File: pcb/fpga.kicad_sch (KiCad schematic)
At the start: 45 parts, among them U1 XC7A50T-FTG256, U2 410-251-B, U3 S70KL1283GABHI020, U4 W25Q128JVS, Y1 ASE-20MHz

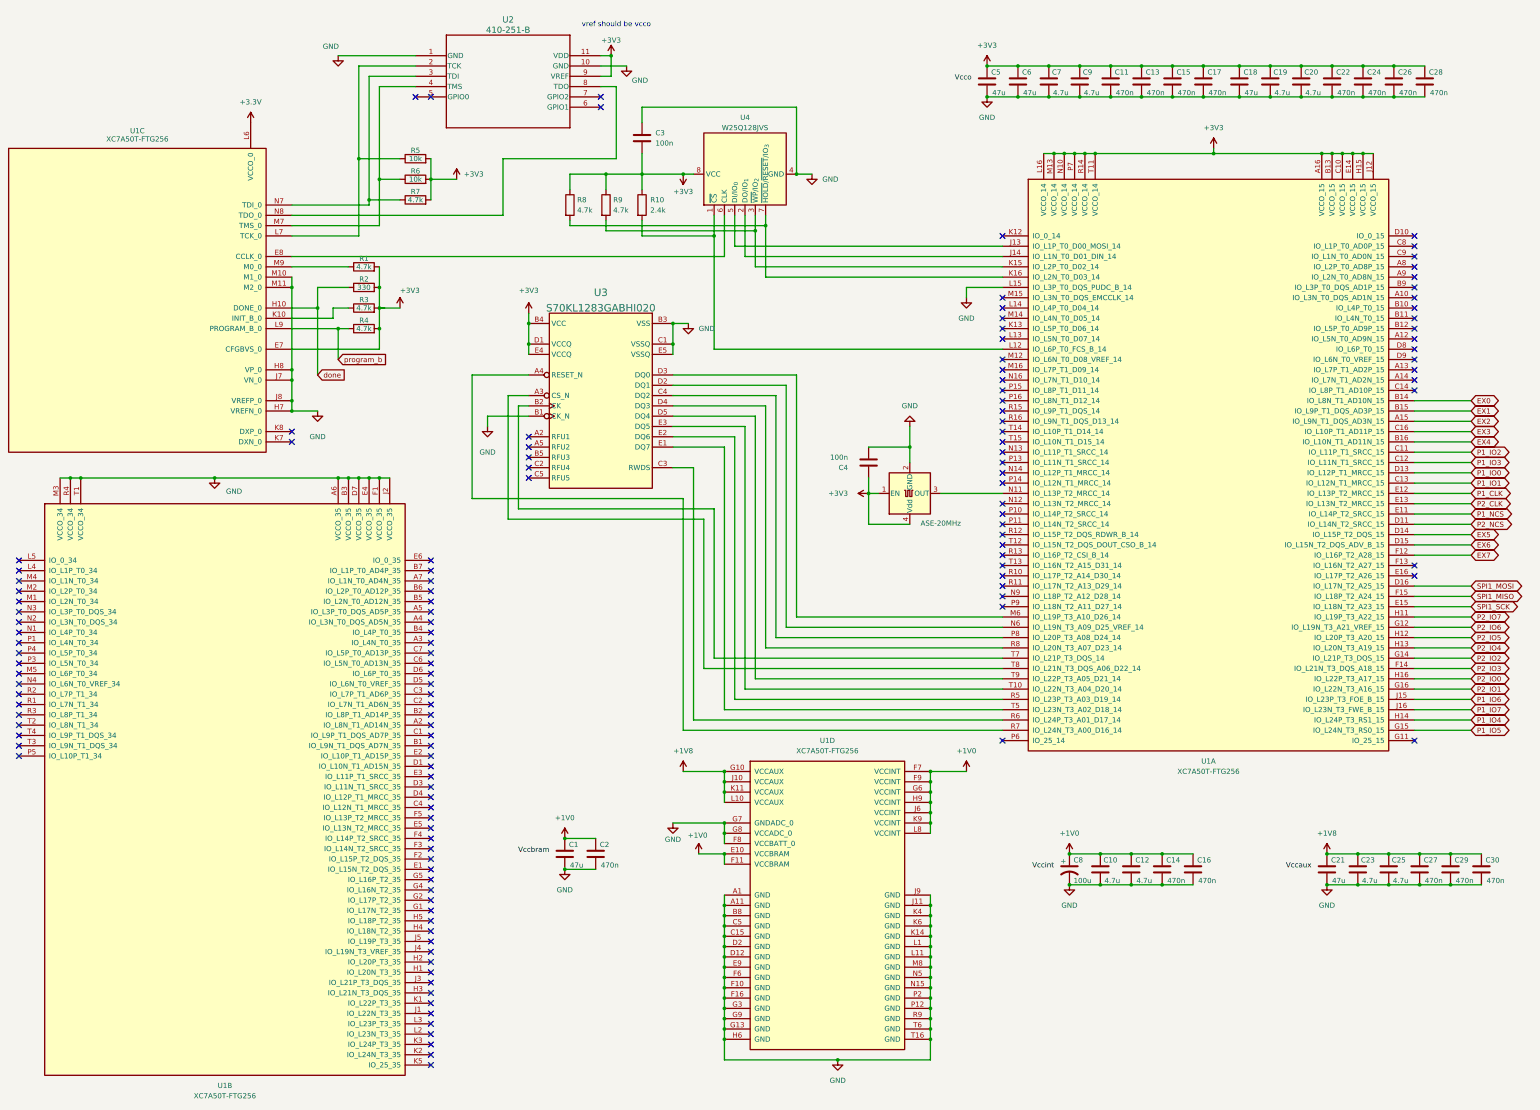
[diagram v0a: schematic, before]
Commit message: fixed erc errors
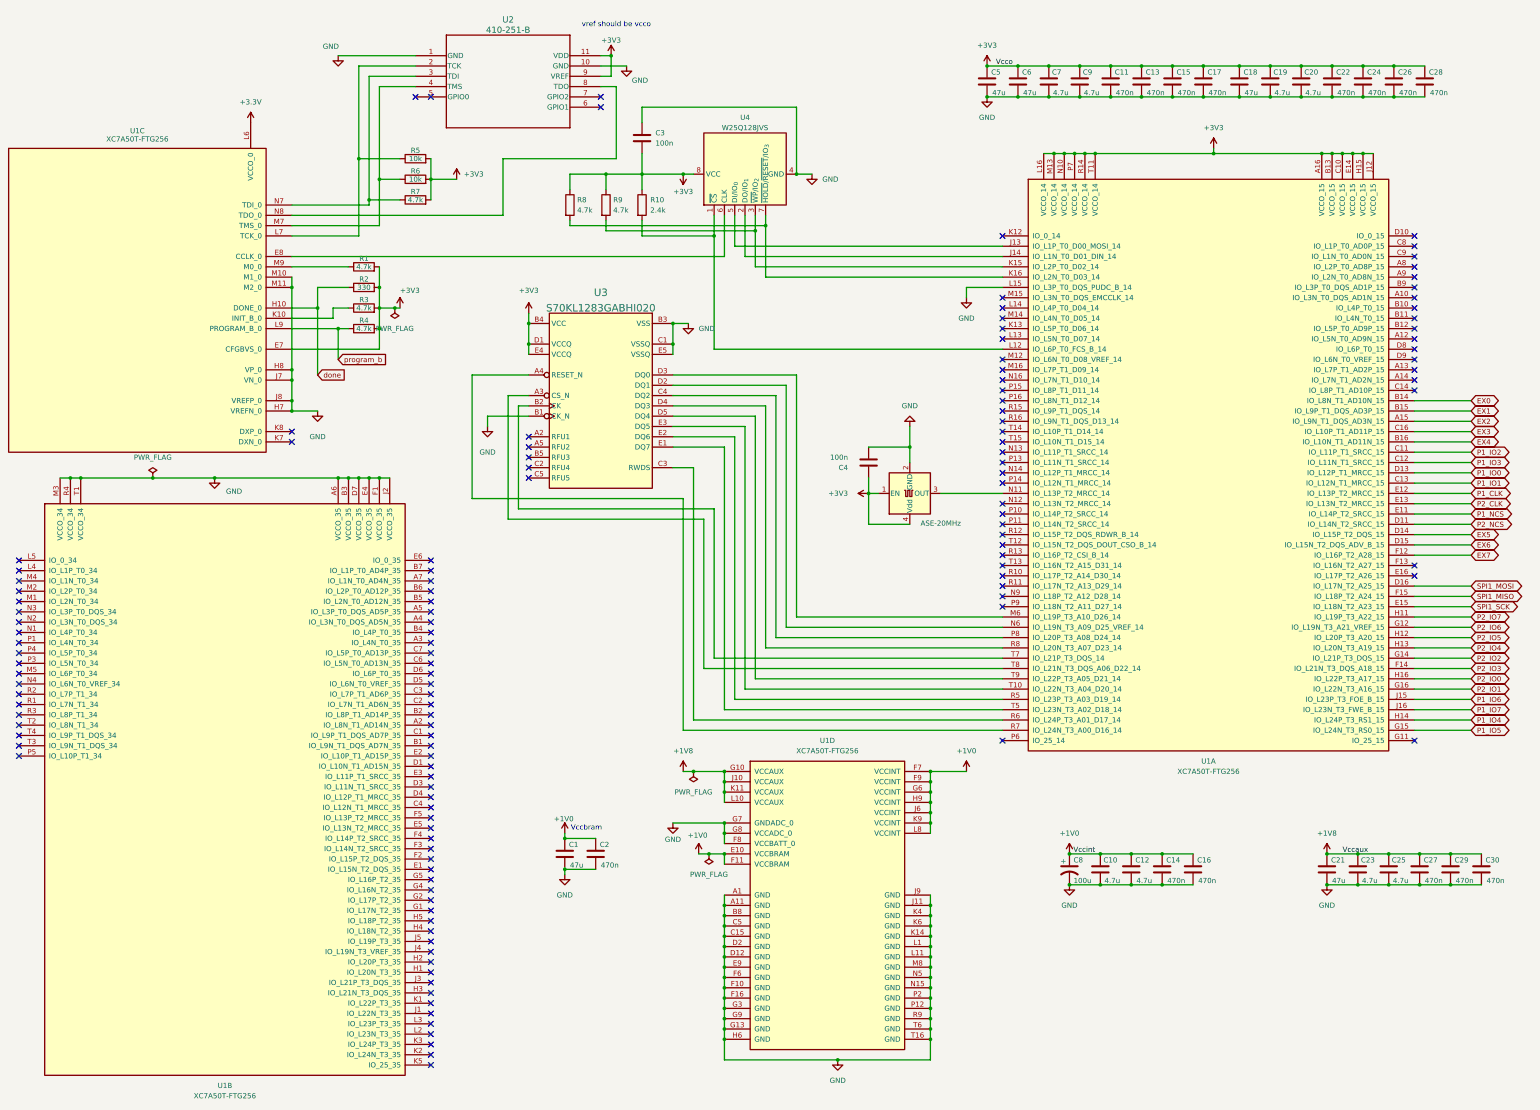
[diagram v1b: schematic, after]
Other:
- note added: "Vccbram"

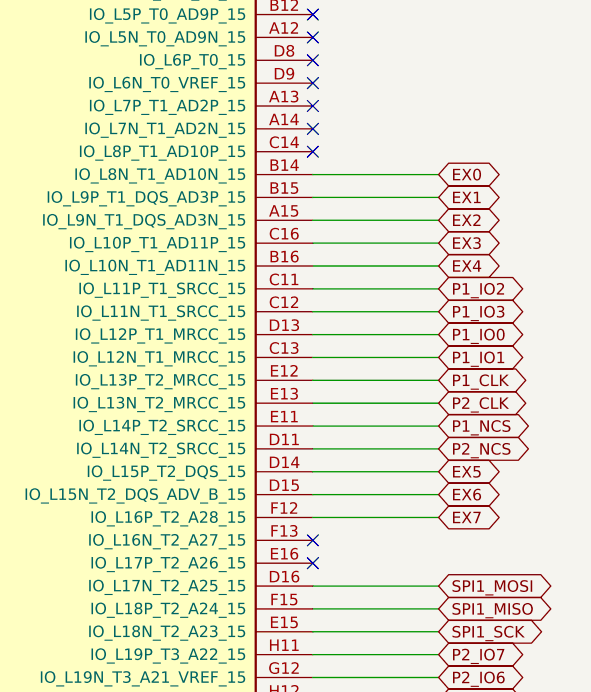
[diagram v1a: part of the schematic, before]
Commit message: pcb: fix erc
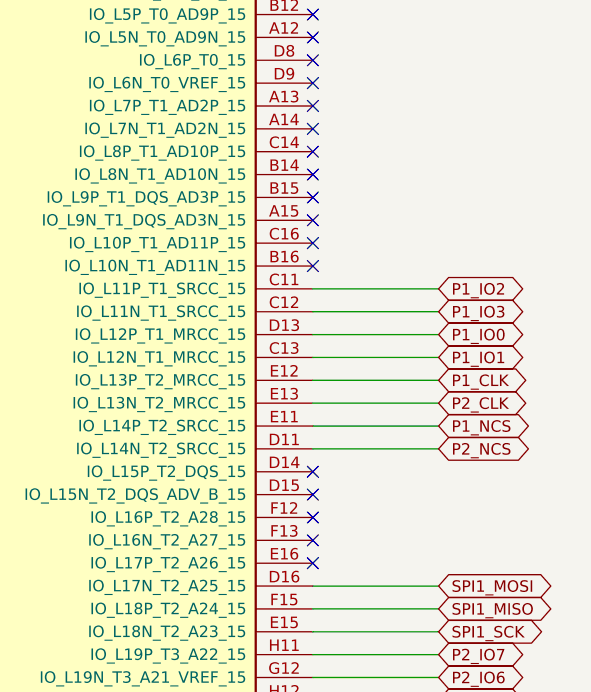
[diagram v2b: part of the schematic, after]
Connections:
- net EX0: no longer names the net of U1.B14 (IO_L8N_T1_AD10N_15)
- net EX1: no longer names the net of U1.B15 (IO_L9P_T1_DQS_AD3P_15)
- net EX2: no longer names the net of U1.A15 (IO_L9N_T1_DQS_AD3N_15)
- net EX3: no longer names the net of U1.C16 (IO_L10P_T1_AD11P_15)
- net EX4: no longer names the net of U1.B16 (IO_L10N_T1_AD11N_15)
- net EX5: no longer names the net of U1.D14 (IO_L15P_T2_DQS_15)
- net EX6: no longer names the net of U1.D15 (IO_L15N_T2_DQS_ADV_B_15)
- net EX7: no longer names the net of U1.F12 (IO_L16P_T2_A28_15)
- no-connect marks 131 -> 139

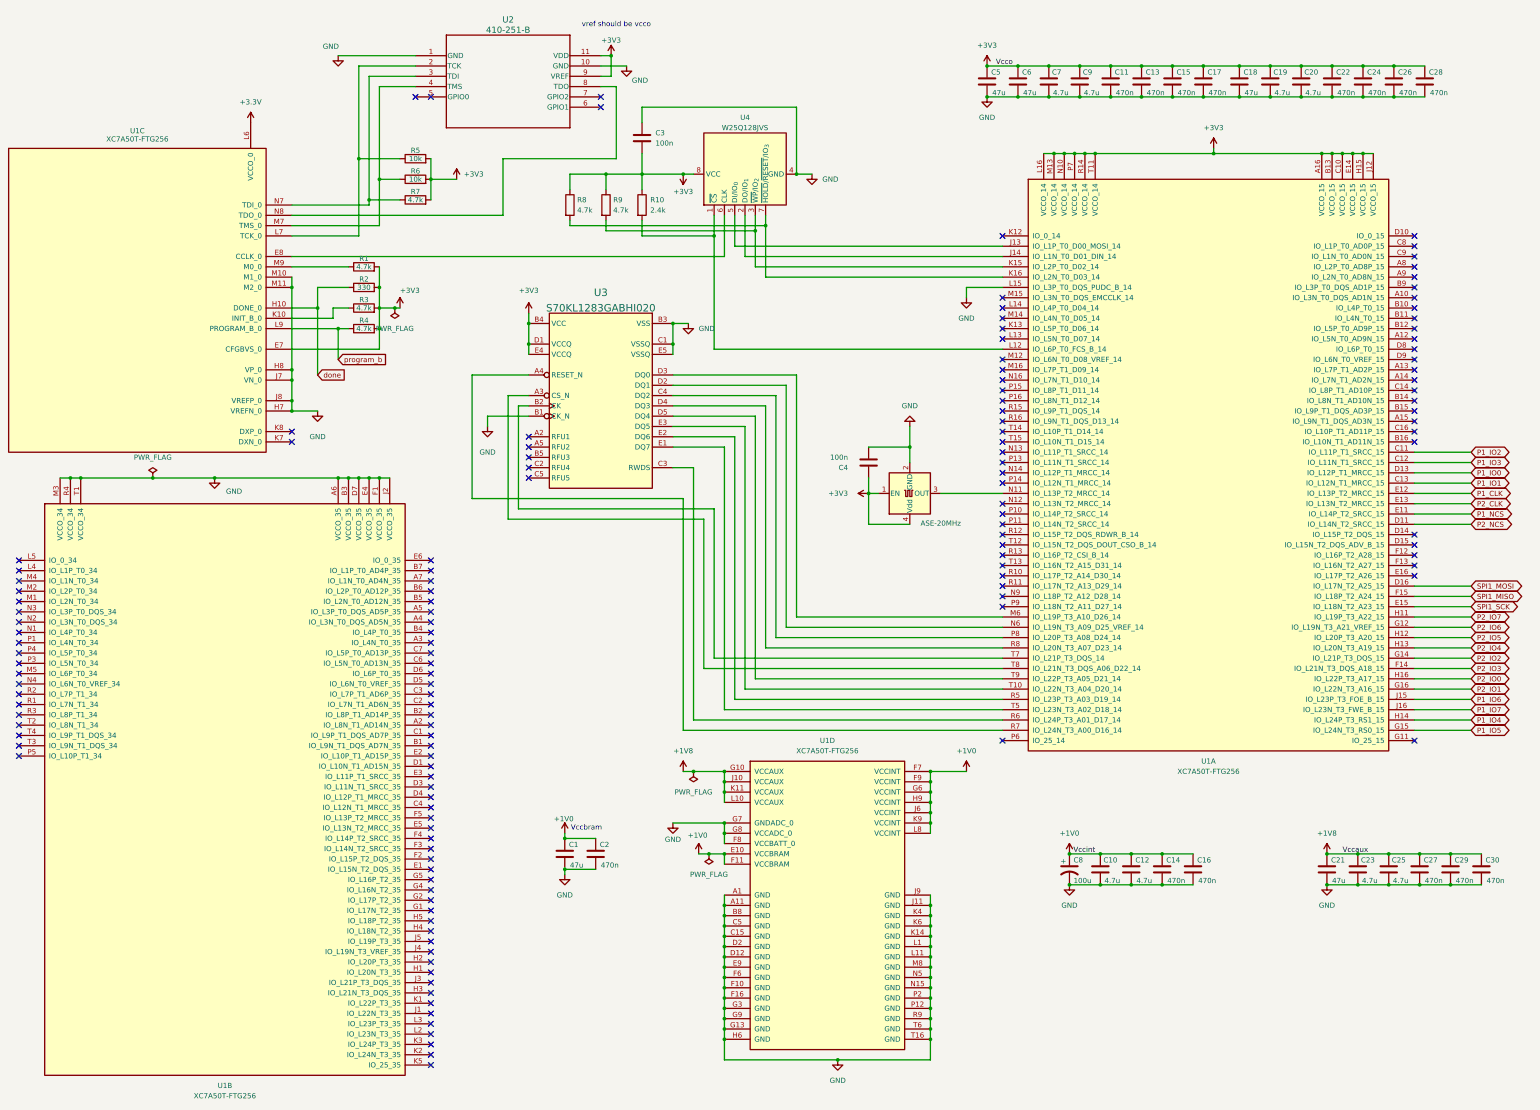
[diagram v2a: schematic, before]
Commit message: pcb: satisfy ERC warnings and errors
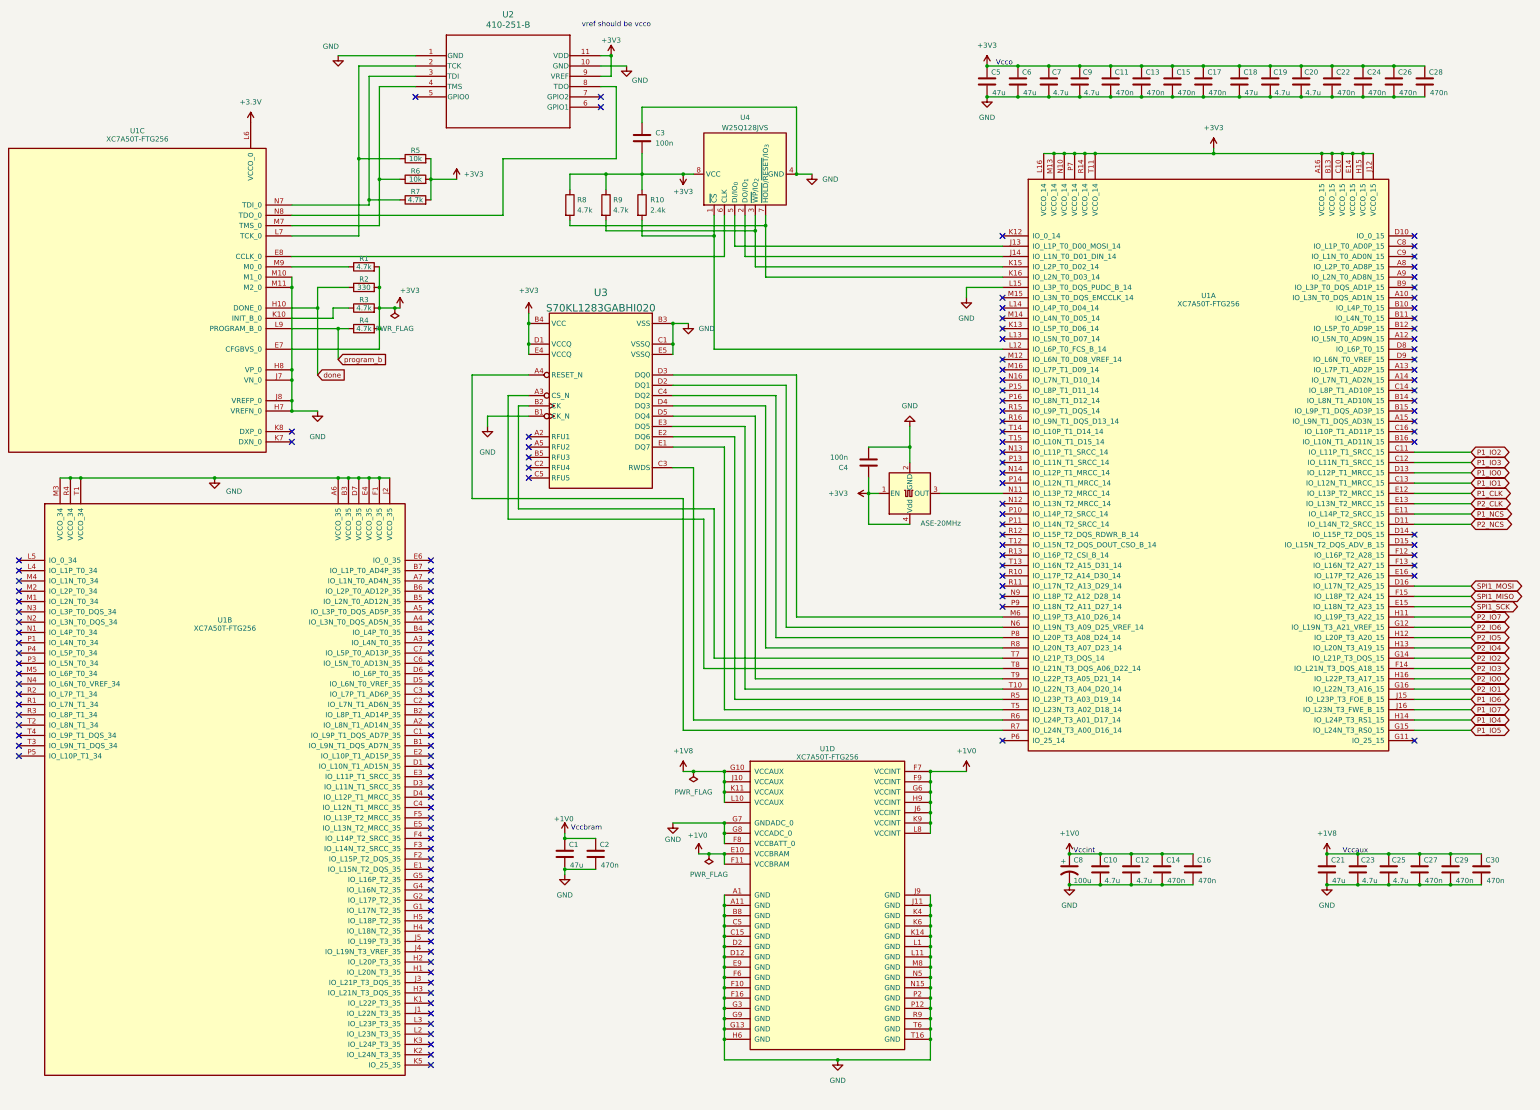
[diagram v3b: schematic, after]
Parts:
- U2: symbol 2026-09-16_13-52-00:410-251-B -> 410-251-B:410-251-B
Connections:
- no-connect marks 139 -> 138
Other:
- note added: "Vccaux"
- note added: "Vccint"
- note added: "Vcco"
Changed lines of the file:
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@@
 		)
 	)
+	(text "Vccaux"
+		(exclude_from_sim no)
+		(at 354.33 222.25 0)
+		(effects
+			(font
+				(size 1.27 1.27)
+				(color 15 7 156 1)
+			)
+			(justify right bottom)
+		)
+	)
+	(text "Vccint"
+		(exclude_from_sim no)
+		(at 287.02 222.25 0)
+		(effects
+			(font
+				(size 1.27 1.27)
+				(color 15 7 156 1)
+			)
+			(justify right bottom)
+		)
+	)
+	(text "Vcco"
+		(exclude_from_sim no)
+		(at 266.7 27.94 0)
+		(effects
+			(font
+				(size 1.27 1.27)
+				(color 15 7 156 1)
+			)
+			(justify right bottom)
+		)
+	)
 	(junction
 		(at 284.48 49.53)
@@
 	)
 	(junction
-		(at 54.61 129.54)
-		(diameter 0)
-		(color 0 0 0 0)
-	)
-	(junction
 		(at 345.44 35.56)
 		(diameter 0)
@@
 	)
 	(no_connect
-		(at 123.19 35.56)
-	)
-	(no_connect
 		(at 147.32 129.54)
 	)
@@
 	(wire
 		(pts
-			(xy 36.83 129.54) (xy 54.61 129.54)
+			(xy 36.83 129.54) (xy 69.85 129.54)
 		)
 		(stroke
@@
 	(wire
 		(pts
-			(xy 54.61 129.54) (xy 69.85 129.54)
-		)
-		(stroke
-			(width 0)
-			(type default)
-		)
-	)
-	(wire
-		(pts
 			(xy 276.86 49.53) (xy 279.4 49.53)
 		)
@@
 		)
 	)
-	(label "Vccaux"
-		(at 354.33 222.25 180)
-		(effects
-			(font
-				(size 1.27 1.27)
-				(color 15 7 156 1)
-			)
-			(justify right bottom)
-		)
-	)
-	(label "Vcco"
-		(at 266.7 27.94 180)
-		(effects
-			(font
-				(size 1.27 1.27)
-				(color 15 7 156 1)
-			)
-			(justify right bottom)
-		)
-	)
-	(label "Vccint"
-		(at 287.02 222.25 180)
-		(effects
-			(font
-				(size 1.27 1.27)
-				(color 15 7 156 1)
-			)
-			(justify right bottom)
-		)
-	)
 	(global_label "P1_CLK"
 		(shape bidirectional)
@@
 	)
 	(symbol
-		(lib_id "power:PWR_FLAG")
-		(at 54.61 129.54 0)
-		(unit 1)
-		(body_style 1)
-		(exclude_from_sim no)
-		(in_bom yes)
-		(on_board yes)
-		(in_pos_files yes)
-		(dnp no)
-		(fields_autoplaced yes)
-		(property "Reference" "#FLG05"
-			(at 54.61 127.635 0)
-			(hide yes)
-			(show_name no)
-			(do_not_autoplace no)
-			(effects
-				(font
-					(size 1.27 1.27)
-				)
-			)
-		)
-		(property "Value" "PWR_FLAG"
-			(at 54.61 124.46 0)
-			(show_name no)
-			(do_not_autoplace no)
-			(effects
-				(font
-					(size 1.27 1.27)
-				)
-			)
-		)
-		(property "Footprint" ""
-			(at 54.61 129.54 0)
-			(hide yes)
-			(show_name no)
-			(do_not_autoplace no)
-			(effects
-				(font
-					(size 1.27 1.27)
-				)
-			)
-		)
-		(property "Datasheet" ""
-			(at 54.61 129.54 0)
-			(hide yes)
-			(show_name no)
-			(do_not_autoplace no)
-			(effects
-				(font
-					(size 1.27 1.27)
-				)
-			)
-		)
-		(property "Description" "Special symbol for telling ERC where power comes from"
-			(at 54.61 129.54 0)
-			(hide yes)
-			(show_name no)
-			(do_not_autoplace no)
-			(effects
-				(font
-					(size 1.27 1.27)
-				)
-			)
-		)
-		(pin "1"
-		)
-		(instances
-			(project "tdt4295"
-				(path "/603dd496-f9c4-4a31-9104-19eec41ebc98/55913984-0b9b-45b1-b632-d56e73135cfc"
-					(reference "#FLG05")
-					(unit 1)
-				)
-			)
-		)
-	)
-	(symbol
 		(lib_id "power:GND")
 		(at 217.17 54.61 0)
@@
 		(fields_autoplaced yes)
 		(property "Reference" "U1"
-			(at 72.39 279.4 0)
+			(at 72.39 164.592 0)
 			(show_name no)
 			(do_not_autoplace no)
@@
 		)
 		(property "Value" "XC7A50T-FTG256"
-			(at 72.39 281.94 0)
+			(at 72.39 166.624 0)
 			(show_name no)
 			(do_not_autoplace no)
@@
 	)
 	(symbol
+		(lib_name "XC7A50T-FTG256_2")
 		(lib_id "FPGA_Xilinx_Artix7:XC7A50T-FTG256")
 		(at 50.8 82.55 0)
@@
 	)
 	(symbol
+		(lib_name "XC7A50T-FTG256_1")
 		(lib_id "FPGA_Xilinx_Artix7:XC7A50T-FTG256")
 		(at 220.98 234.95 0)
@@
 		(fields_autoplaced yes)
 		(property "Reference" "U1"
-			(at 220.98 194.31 0)
+			(at 220.98 196.342 0)
 			(show_name no)
 			(do_not_autoplace no)
@@
 		)
 		(property "Value" "XC7A50T-FTG256"
-			(at 220.98 196.85 0)
+			(at 220.98 198.374 0)
 			(show_name no)
 			(do_not_autoplace no)
@@
 	)
 	(symbol
+		(lib_name "XC7A50T-FTG256_3")
 		(lib_id "FPGA_Xilinx_Artix7:XC7A50T-FTG256")
 		(at 314.96 123.19 0)
@@
 		(fields_autoplaced yes)
 		(property "Reference" "U1"
-			(at 314.96 199.39 0)
+			(at 314.96 84.582 0)
 			(show_name no)
 			(do_not_autoplace no)
@@
 		)
 		(property "Value" "XC7A50T-FTG256"
-			(at 314.96 201.93 0)
+			(at 314.96 86.614 0)
 			(show_name no)
 			(do_not_autoplace no)
@@
 	)
 	(symbol
-		(lib_id "2026-09-16_13-52-00:410-251-B")
+		(lib_id "410-251-B:410-251-B")
 		(at 119.38 25.4 0)
 		(unit 1)
@@
 		(fields_autoplaced yes)
 		(property "Reference" "U2"
-			(at 142.24 16.51 0)
+			(at 142.24 15.24 0)
 			(show_name no)
 			(do_not_autoplace no)
@@
 		)
 		(property "Value" "410-251-B"
-			(at 142.24 19.05 0)
+			(at 142.24 17.78 0)
 			(show_name no)
 			(do_not_autoplace no)
